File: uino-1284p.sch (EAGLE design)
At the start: 59 parts, among them J1 Micro USB, J2 M03X2, J3 CON_TERMINAL_BLOCK_02-5MM, J4 M03X2, J5 IO, U1 ATMEGA8U2AU, U2 LD117AS50TR, U3 ATMEGA1284AU, X1 16MHz, X2 16MHz

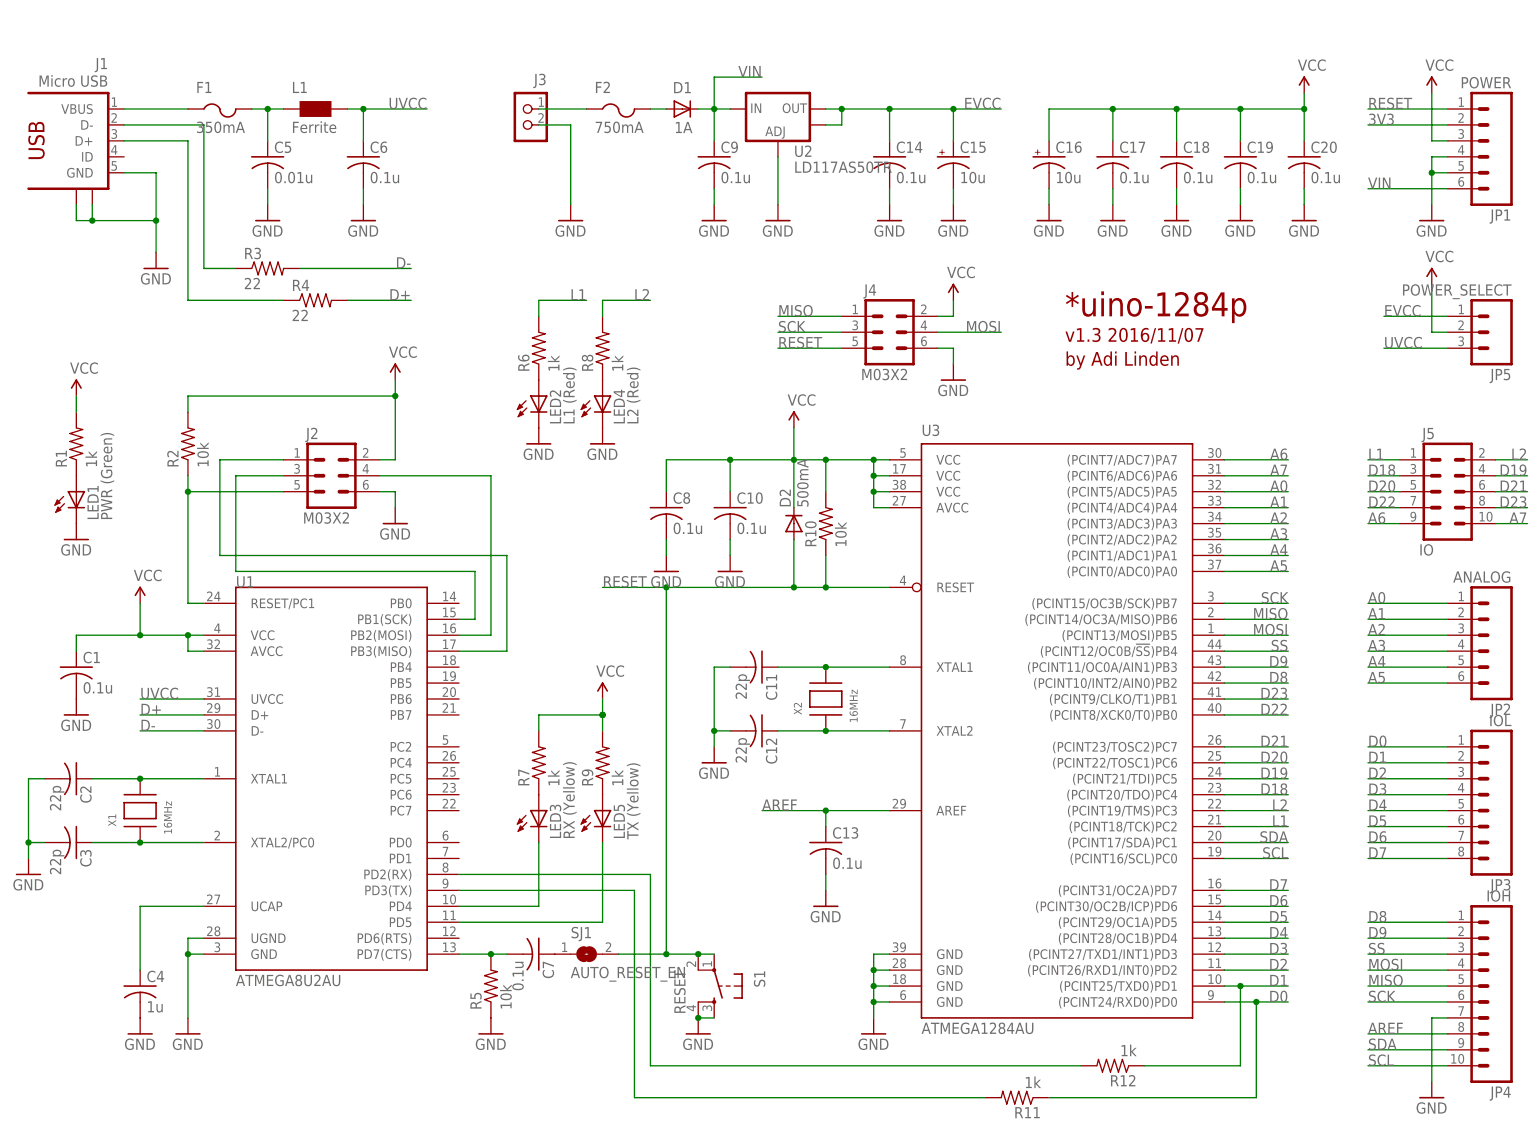
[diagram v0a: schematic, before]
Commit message: Replaced reverse polarity schottky with P-FET.
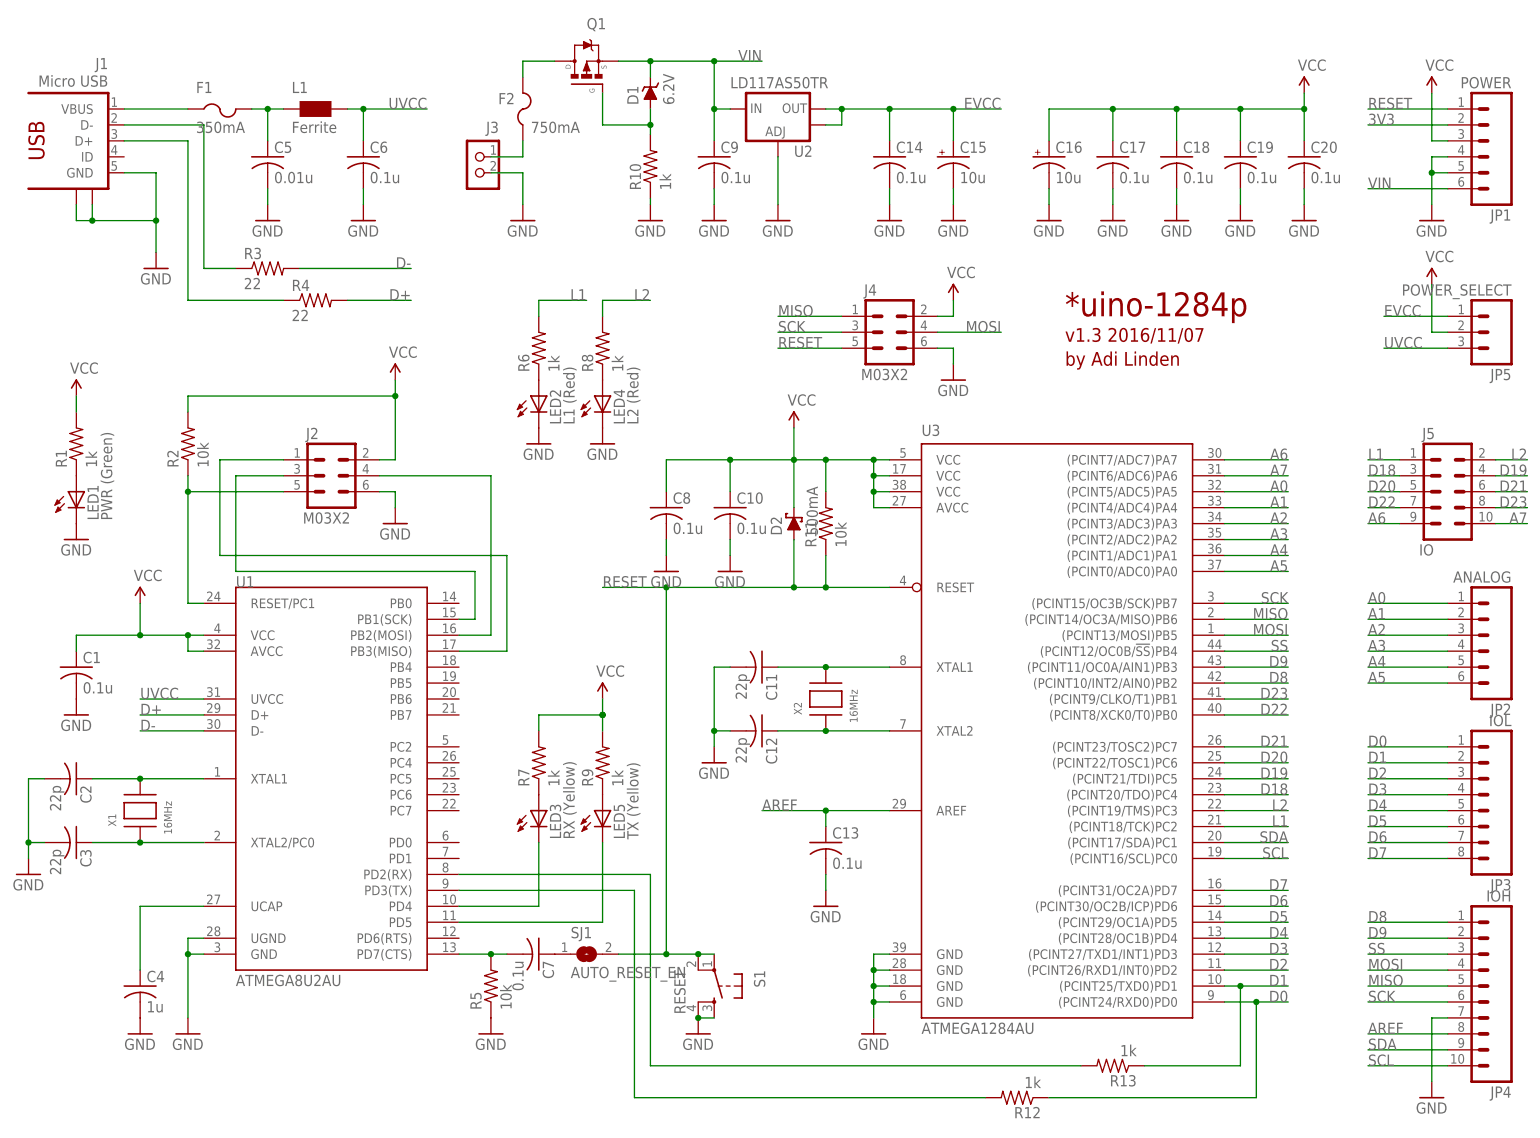
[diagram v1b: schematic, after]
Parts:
- added Q1: MMBF0202PLT1, transistor-fet:MMBF0202PLT1
- added R13: 1k, rcl:R-US_R0805
- D1: value 1A -> 6.2V; device diode:MBR0520LT -> diode:BZX384
- D2: device diode:MBR0520LT -> diode:SCHOTTKY-DIODESOD323
- R10: value 10k -> 1k
- R11: value 1k -> 10k
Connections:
- new net N$18: D1.A, Q1.G, R10.2
- net D0: now also R12.1; no longer R11.1
- net D1: now also R13.1; no longer R12.1
- net GND: now also R10.1
- net N$1: now also Q1.D; no longer D1.A
- net N$6: now also R12.2; no longer R11.2
- net N$7: now also R13.2; no longer R12.2
- net RESET: now also R11.1; no longer R10.1
- net VCC: now also R11.2; no longer R10.2
- net VIN: now also Q1.S
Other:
- moved on the sheet: F2, J3, R10, R11, R12

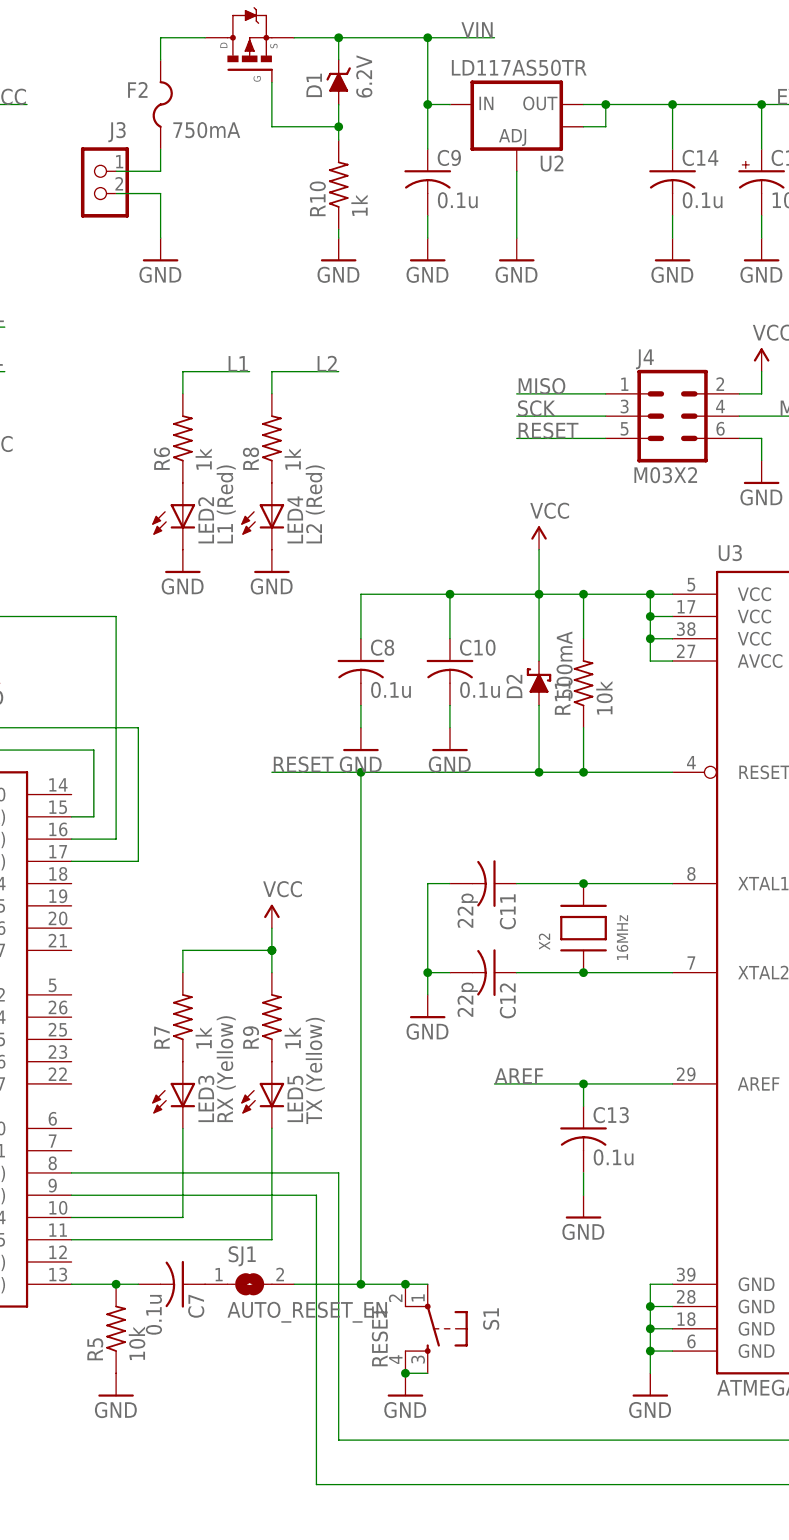
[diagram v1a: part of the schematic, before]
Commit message: Fixed values and numbering.
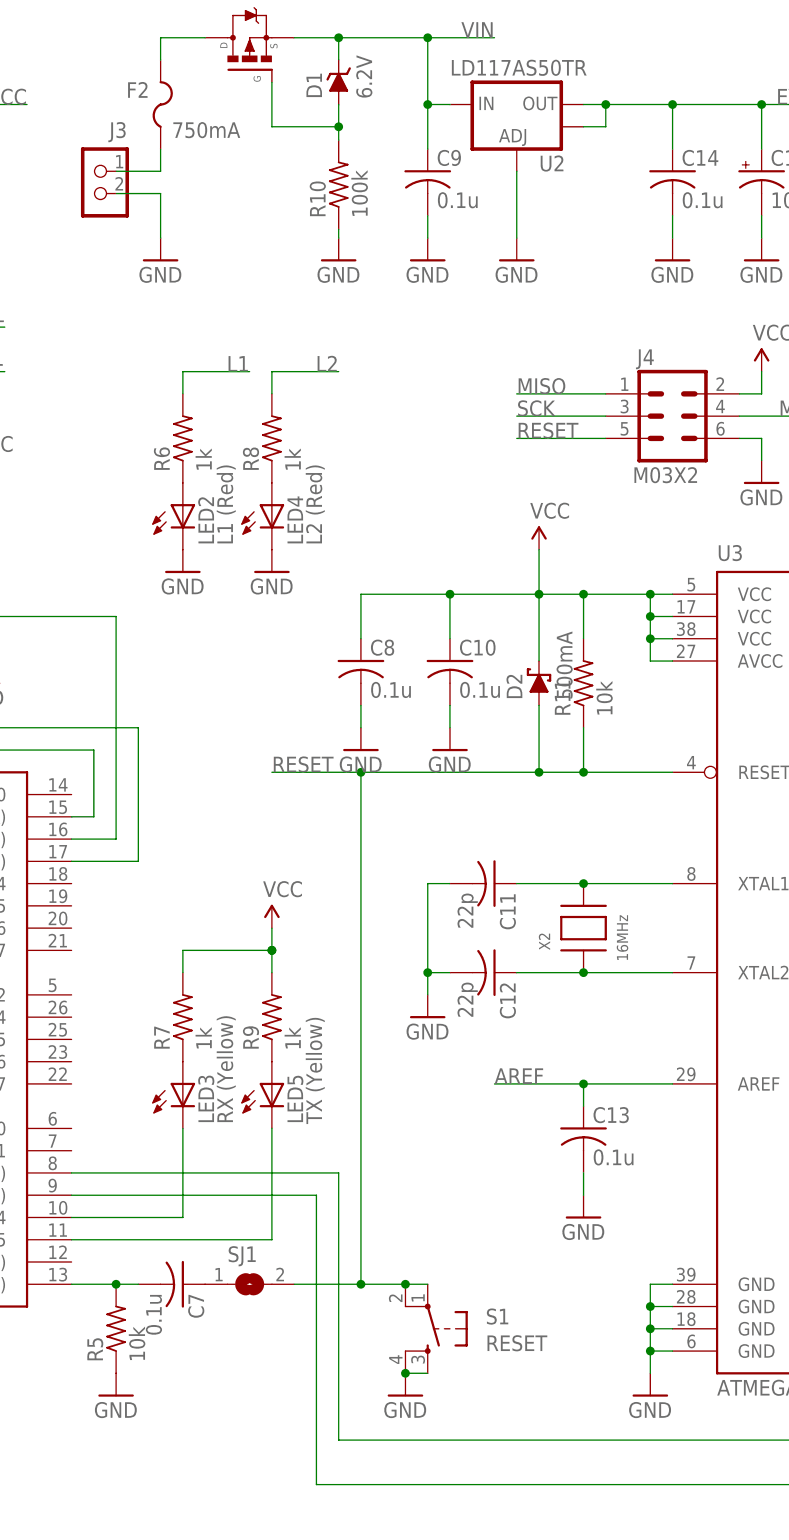
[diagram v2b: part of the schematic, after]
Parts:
- R10: value 1k -> 100k
- SJ1: value AUTO_RESET_EN -> (none)
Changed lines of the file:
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@@
 <part name="GND29" library="supply1" deviceset="GND" device=""/>
 <part name="GND16" library="supply1" deviceset="GND" device=""/>
-<part name="SJ1" library="jumper" deviceset="SJ" device="" value="AUTO_RESET_EN"/>
+<part name="SJ1" library="jumper" deviceset="SJ" device=""/>
 <part name="C20" library="rcl" deviceset="C-US" device="C0805" value="0.1u"/>
 <part name="GND30" library="supply1" deviceset="GND" device=""/>
@@
 <part name="Q1" library="transistor-fet" deviceset="MMBF0202P*" device="" technology="LT1" value=""/>
 <part name="D1" library="diode" deviceset="BZX384*" device="" value="6.2V"/>
-<part name="R10" library="rcl" deviceset="R-US_" device="R0805" value="1k"/>
+<part name="R10" library="rcl" deviceset="R-US_" device="R0805" value="100k"/>
 <part name="GND14" library="supply1" deviceset="GND" device=""/>
 </parts>
@@
 <instance part="C13" gate="G$1" x="134.62" y="53.34"/>
 <instance part="GND21" gate="1" x="134.62" y="43.18"/>
-<instance part="S1" gate="S" x="116.84" y="30.48" rot="R270"/>
+<instance part="S1" gate="S" x="116.84" y="30.48" smashed="yes" rot="R270">
+<attribute name="NAME" x="123.444" y="30.988" size="1.778" layer="95"/>
+<attribute name="VALUE" x="123.444" y="27.94" size="1.778" layer="96"/>
+</instance>
 <instance part="R13" gate="G$1" x="180.34" y="17.78" rot="R180"/>
 <instance part="R12" gate="G$1" x="165.1" y="12.7" rot="R180"/>
